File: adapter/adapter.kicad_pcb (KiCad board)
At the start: 2 copper layers, 93.5 x 50.9 mm, 61 parts, among them J1 Serial, J10 Ribbon, J11 Ribbon, J12 Ribbon, J13 serial, J14 serial, J2 Serial, J3 battery charge, J4 RGB, J5 RGB, J6 battery charge, J7 trackball, J8 trackball, J9 Ribbon, SW1 SW_SPST, SW2 SW_SPST, SW3 SW_SPDT, SW4 SW_SPDT, U1 eliteC, U2 eliteC

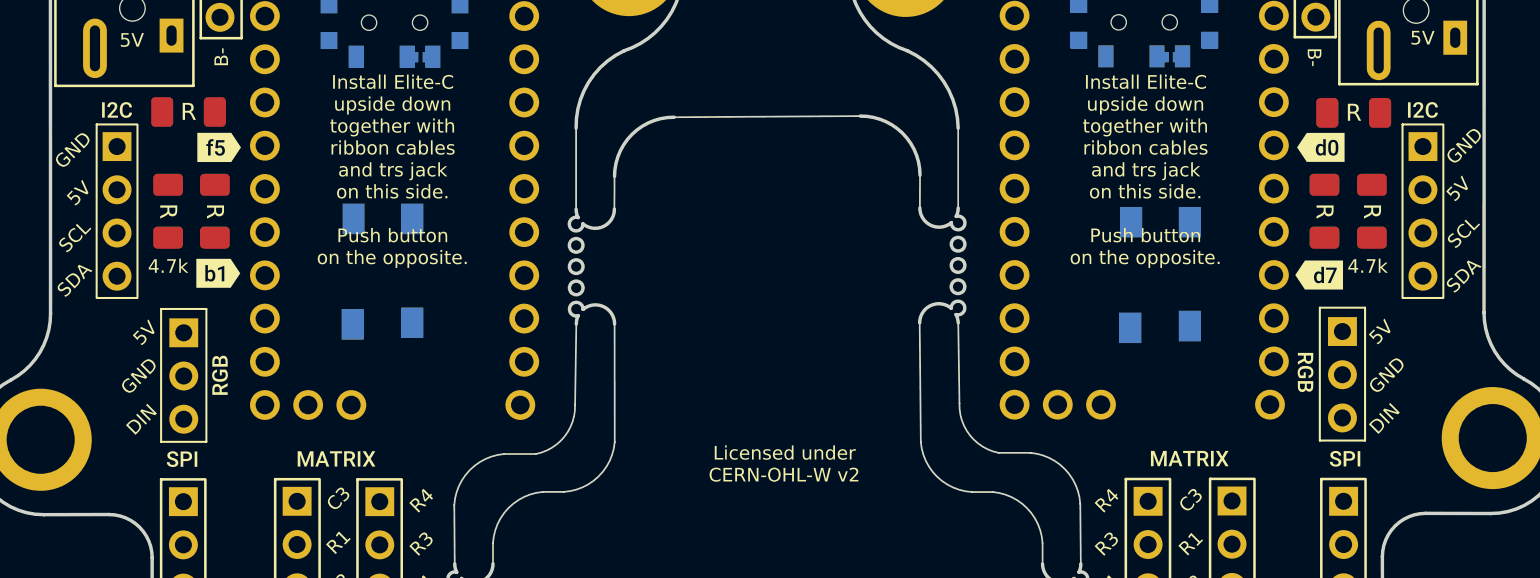
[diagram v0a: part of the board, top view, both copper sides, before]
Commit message: pcb: update some silkscreen
Signed-off-by: Anant Thazhemadam <anant.thazhemadam@gmail.com>
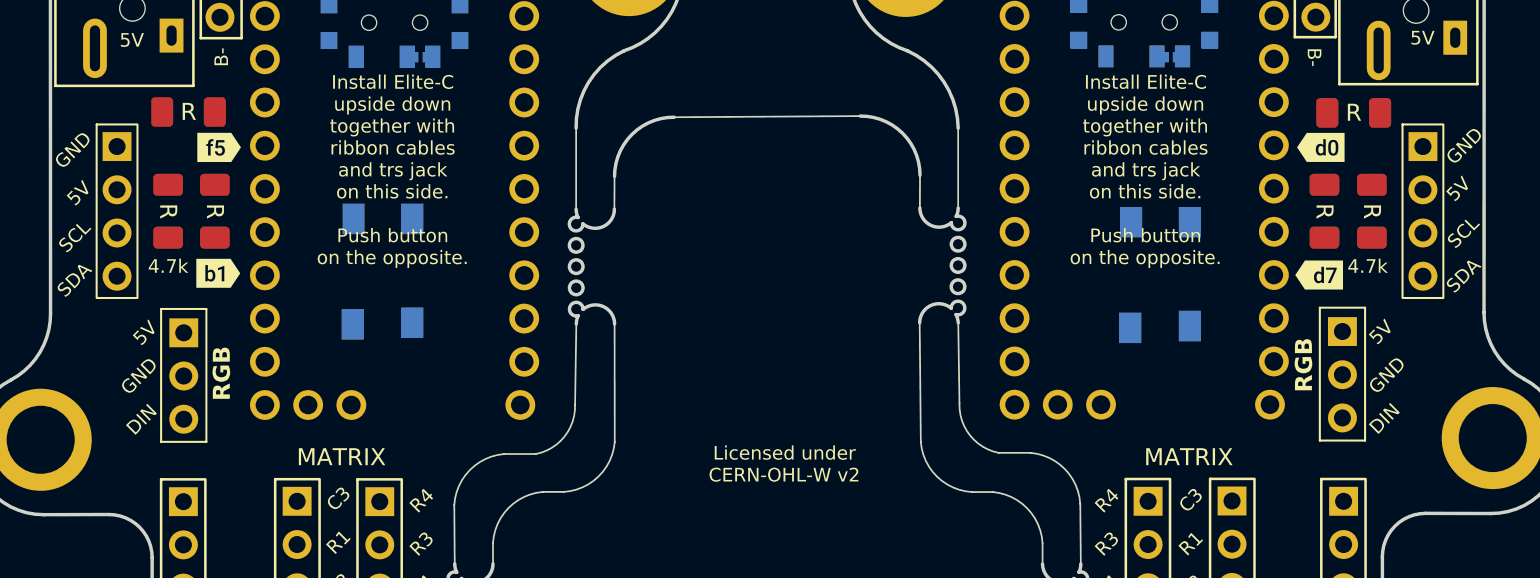
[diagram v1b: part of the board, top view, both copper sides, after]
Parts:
- removed G***: LOGO, LOGO
- removed kibuzzard-61F01940 (x4): G***, kibuzzard-61F01940
- removed kibuzzard-61F01957 (x4): G***, kibuzzard-61F01957
- removed kibuzzard-61F019CB (x4): G***, kibuzzard-61F019CB
- removed kibuzzard-620B8D91 (x4): G***, kibuzzard-620B8D91
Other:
- board text added: "MATRIX"
- board text added: "RGB"
- board text removed: "2022 QUENTIN LEBASTARD AND STEFAN KERKMANN"
- board text removed: "BASTARDKB.COM"
- board text removed: "ELITE-C HOLDER 2.1"
- board text removed: "GITHUB.COM/BASTARDKB"
- board text removed: "Special thanks to: Drashna, Freznel Karl"

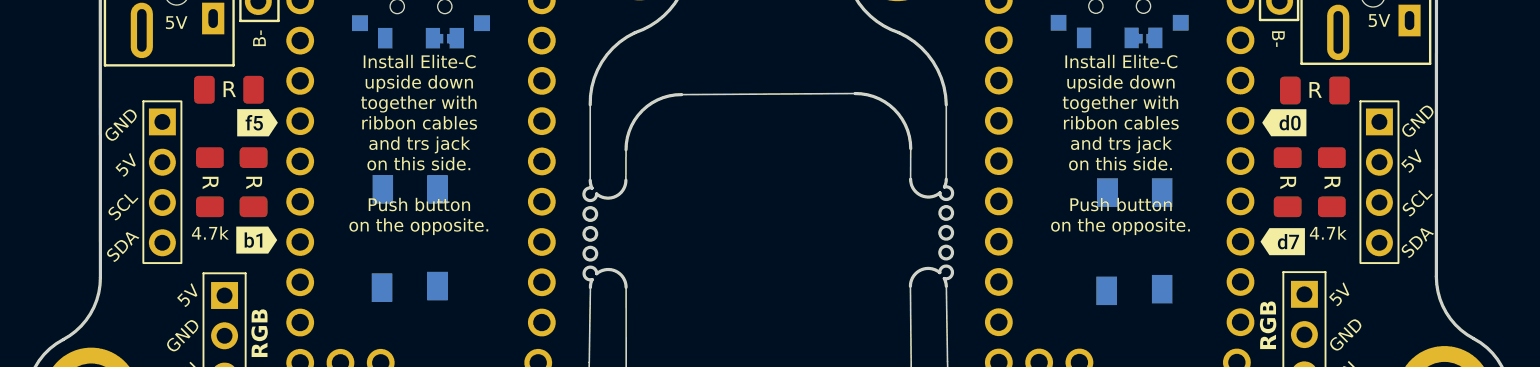
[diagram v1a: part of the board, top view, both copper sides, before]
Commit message: pcb: remove I2C breakouts
Signed-off-by: Anant Thazhemadam <anant.thazhemadam@gmail.com>
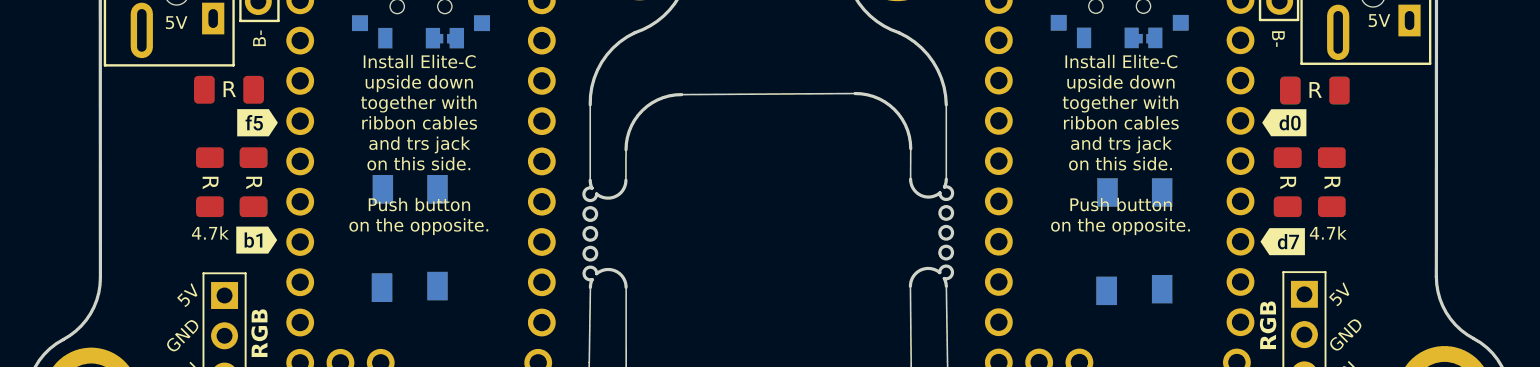
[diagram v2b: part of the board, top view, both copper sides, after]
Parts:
- removed J13, J14: serial, library:PinHeader_1x04_P2.54mm_Vertical
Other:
- board text removed: "SCL"
- board text removed: "SDA"

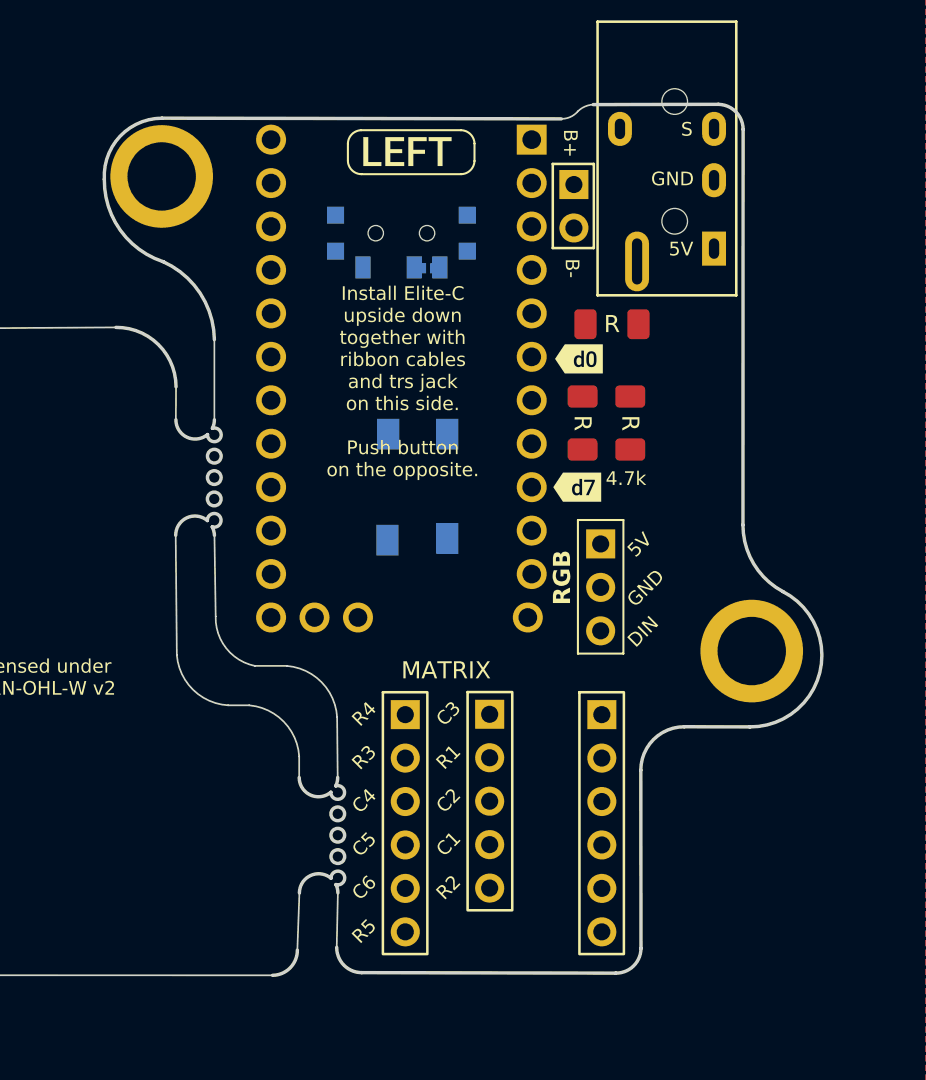
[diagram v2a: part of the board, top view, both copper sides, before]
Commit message: pcb(edge-cuts): remove right hand side edge cuts
Signed-off-by: Anant Thazhemadam <anant.thazhemadam@gmail.com>
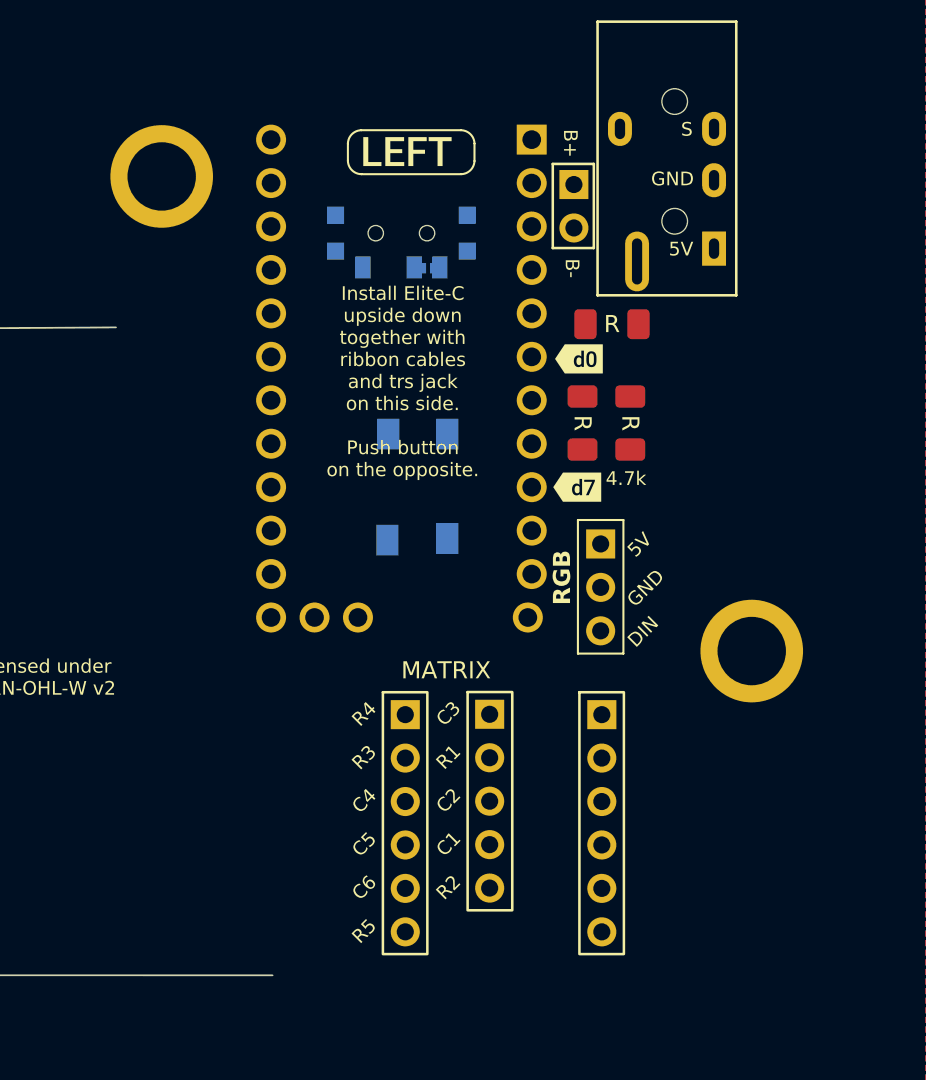
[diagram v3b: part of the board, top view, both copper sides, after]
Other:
- board size 93.5 x 50.9 mm -> 61.4 x 50.9 mm

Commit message: pcb(edge-cuts): symmetry!
Signed-off-by: Anant Thazhemadam <anant.thazhemadam@gmail.com>
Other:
- board size 61.4 x 50.9 mm -> 61.4 x 50.8 mm
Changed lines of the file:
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@@
 	)
 	(gr_arc
-		(start 113.341486 91.773749)
-		(mid 112.713926 94.049213)
-		(end 111.001486 95.673749)
+		(start 113.331485 91.773751)
+		(mid 112.705363 94.044066)
+		(end 110.996809 95.664932)
 		(stroke
 			(width 0.2)
@@
 	(gr_line
 		(start 137.096291 106.475003)
-		(end 137.07 103.02)
+		(end 137.096291 103.0199)
+		(locked yes)
 		(stroke
 			(width 0.1)
@@
 	)
 	(gr_line
-		(start 120.775358 117.982362)
-		(end 135.631351 117.953354)
+		(start 120.736124 117.982362)
+		(end 135.631379 117.982362)
 		(stroke
 			(width 0.2)
@@
 	)
 	(gr_line
-		(start 141.87 100.02)
-		(end 139.998866 100.02)
+		(start 141.870036 100.116191)
+		(end 139.998902 100.116191)
+		(locked yes)
 		(stroke
 			(width 0.1)
@@
 		(start 144.230005 85.631645)
 		(end 144.230005 80.872466)
-		(stroke
-			(width 0.1)
-			(type solid)
-		)
-		(layer "Edge.Cuts")
-	)
-	(gr_line
-		(start 112.943471 103.585074)
-		(end 116.773949 103.576051)
-		(stroke
-			(width 0.2)
-			(type solid)
+		(locked yes)
+		(stroke
+			(width 0.1)
+			(type solid)
+		)
+		(layer "Edge.Cuts")
+	)
+	(gr_line
+		(start 112.938794 103.576257)
+		(end 116.769283 103.576257)
+		(locked yes)
+		(stroke
+			(width 0.2)
+			(type solid)
+		)
+		(layer "Edge.Cuts")
+	)
+	(gr_arc
+		(start 120.736124 117.985765)
+		(mid 119.709142 117.560375)
+		(end 119.283752 116.533393)
+		(stroke
+			(width 0.2)
+			(type default)
 		)
 		(layer "Edge.Cuts")
@@
 	)
 	(gr_arc
-		(start 144.17 97.12)
-		(mid 143.551367 98.991429)
-		(end 141.87 100.02)
-		(stroke
-			(width 0.1)
-			(type solid)
+		(start 137.09335 116.477233)
+		(mid 136.652508 117.541521)
+		(end 135.58822 117.982363)
+		(locked yes)
+		(stroke
+			(width 0.1)
+			(type default)
 		)
 		(layer "Edge.Cuts")
@@
 	)
 	(gr_line
-		(start 137.108072 113.224991)
-		(end 137.09335 116.477233)
+		(start 137.09335 113.224991)
+		(end 137.09335 116.477266)
+		(locked yes)
 		(stroke
 			(width 0.1)
@@
 	)
 	(gr_line
-		(start 144.17 97.12)
+		(start 144.241822 97.744405)
 		(end 144.241786 92.381633)
+		(locked yes)
 		(stroke
 			(width 0.1)
@@
 	)
 	(gr_arc
+		(start 116.769283 103.576258)
+		(mid 118.549131 104.317198)
+		(end 119.283752 106.099664)
+		(locked yes)
+		(stroke
+			(width 0.2)
+			(type default)
+		)
+		(layer "Edge.Cuts")
+	)
+	(gr_arc
 		(start 137.210084 106.966079)
 		(mid 137.125328 106.726997)
@@
 		(layer "Edge.Cuts")
 	)
+	(gr_arc
+		(start 137.096291 103.0199)
+		(mid 137.94638 100.967056)
+		(end 139.998902 100.116191)
+		(locked yes)
+		(stroke
+			(width 0.1)
+			(type default)
+		)
+		(layer "Edge.Cuts")
+	)
 	(gr_line
 		(start 147.305648 67.994096)
-		(end 123.961303 68.03306)
+		(end 123.96127 67.994096)
+		(locked yes)
 		(stroke
 			(width 0.2)
@@
 	(gr_line
 		(start 122.1 67.2)
-		(end 114.781486 67.183749)
+		(end 114.785236 67.199999)
+		(locked yes)
 		(stroke
 			(width 0.2)
@@
 	)
 	(gr_arc
-		(start 112.943471 103.585074)
-		(mid 108.84637 100.396774)
-		(end 111.001486 95.673749)
+		(start 112.938794 103.576257)
+		(mid 108.841727 100.387977)
+		(end 110.996809 95.664932)
 		(stroke
 			(width 0.2)
@@
 	(gr_arc
 		(start 113.331486 68.653749)
-		(mid 113.754912 67.621278)
-		(end 114.781486 67.183749)
-		(stroke
-			(width 0.2)
-			(type solid)
+		(mid 113.75728 67.625793)
+		(end 114.785236 67.199999)
+		(locked yes)
+		(stroke
+			(width 0.2)
+			(type default)
 		)
 		(layer "Edge.Cuts")
@@
 	)
 	(gr_line
-		(start 119.302824 116.533393)
-		(end 119.313949 106.116051)
-		(stroke
-			(width 0.2)
-			(type solid)
-		)
-		(layer "Edge.Cuts")
-	)
-	(gr_arc
-		(start 137.09335 116.477233)
-		(mid 136.67 117.52)
-		(end 135.631351 117.953354)
-		(stroke
-			(width 0.2)
-			(type solid)
-		)
-		(layer "Edge.Cuts")
-	)
-	(gr_arc
-		(start 120.775358 117.982362)
-		(mid 119.738483 117.563374)
-		(end 119.302824 116.533393)
+		(start 119.283752 116.533393)
+		(end 119.283752 106.099664)
+		(locked yes)
 		(stroke
 			(width 0.2)
@@
 		(stroke
 			(width 0.1)
-			(type solid)
-		)
-		(layer "Edge.Cuts")
-	)
-	(gr_arc
-		(start 116.773949 103.576051)
-		(mid 118.57 104.32)
-		(end 119.313949 106.116051)
-		(stroke
-			(width 0.2)
 			(type solid)
 		)
@@
 	)
 	(gr_arc
+		(start 144.241822 97.744405)
+		(mid 143.547142 99.421511)
+		(end 141.870036 100.116191)
+		(locked yes)
+		(stroke
+			(width 0.1)
+			(type default)
+		)
+		(layer "Edge.Cuts")
+	)
+	(gr_arc
 		(start 137.108072 113.224991)
 		(mid 137.136229 112.972898)
@@
 	)
 	(gr_arc
-		(start 137.07 103.02)
-		(mid 137.974475 100.973319)
-		(end 139.998866 100.02)
-		(stroke
-			(width 0.1)
-			(type solid)
-		)
-		(layer "Edge.Cuts")
-	)
-	(gr_arc
 		(start 140.903204 118.03399)
 		(mid 139.873005 117.596021)
@@
 	(gr_line
 		(start 113.331486 68.653749)
-		(end 113.341486 91.773749)
-		(stroke
-			(width 0.2)
+		(end 113.331486 91.773751)
+		(locked yes)
+		(stroke
+			(width 0.2)

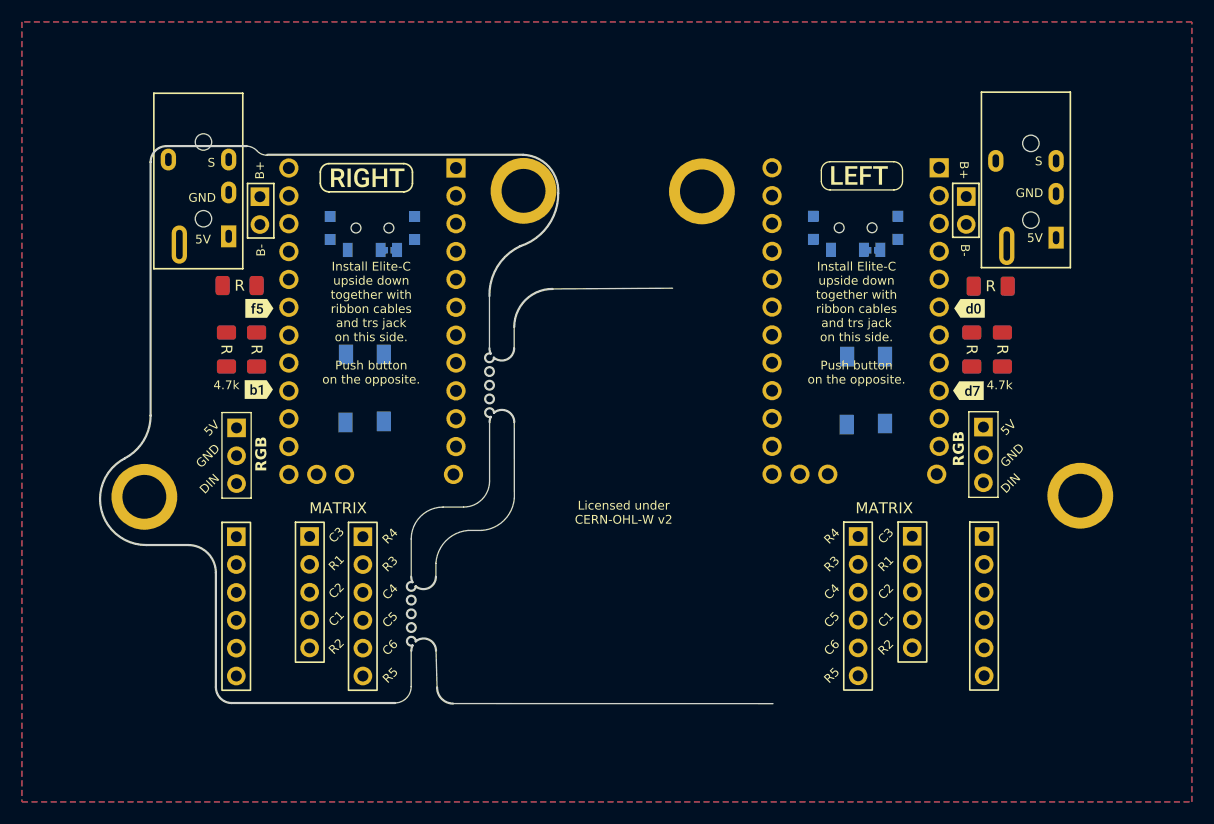
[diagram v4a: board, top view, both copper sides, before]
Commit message: pcb(edge-cuts): true symmetry! add rhs too
Signed-off-by: Anant Thazhemadam <anant.thazhemadam@gmail.com>
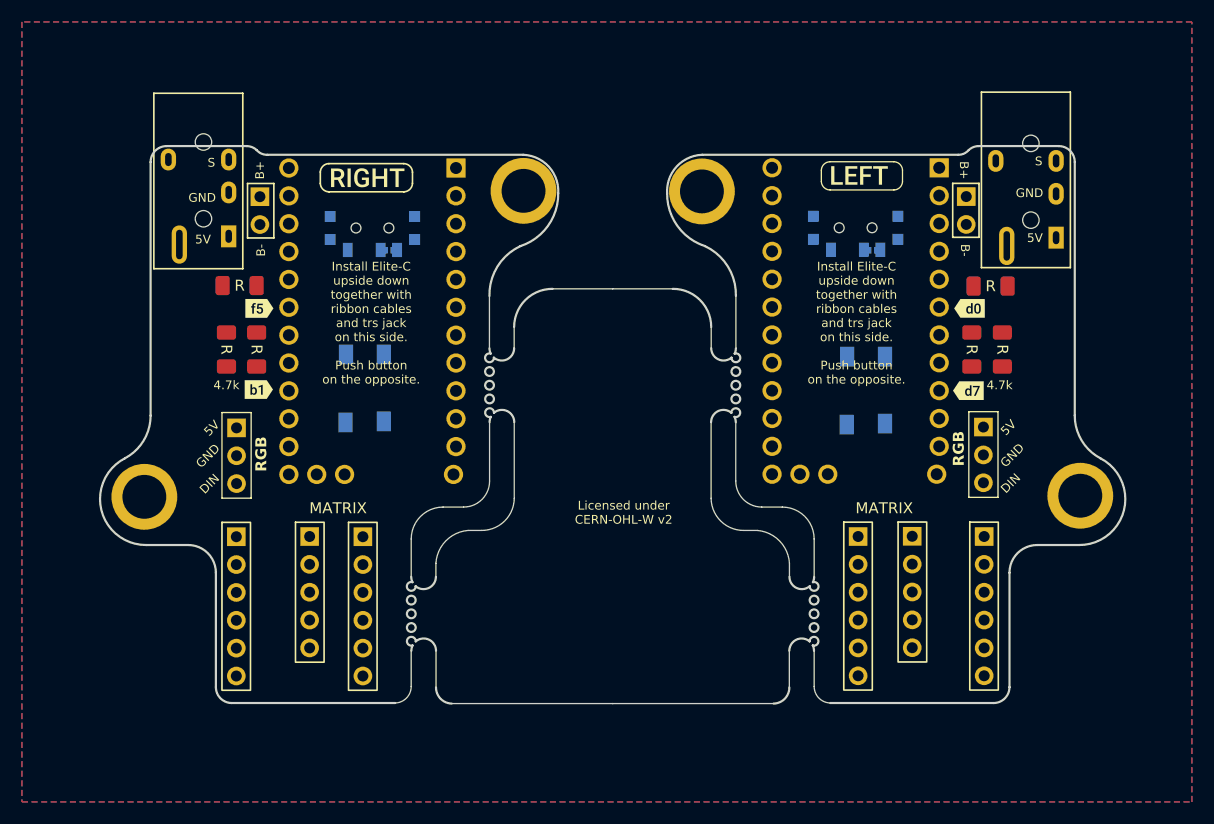
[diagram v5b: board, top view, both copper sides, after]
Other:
- board size 61.4 x 50.8 mm -> 93.5 x 50.8 mm
- board text removed: "C1"
- board text removed: "C2"
- board text removed: "C3"
- board text removed: "C4"
- board text removed: "C5"
- board text removed: "C6"
- board text removed: "R1"
- board text removed: "R2"
- board text removed: "R3"
- board text removed: "R4"
- board text removed: "R5"
